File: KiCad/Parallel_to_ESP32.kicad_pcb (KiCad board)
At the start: 2 copper layers, 47 x 50 mm, 9 parts, among them J1 DB25_Male, J3 Micro_SD_Card_Socket, U1 ESP32-DEVKIT-V1

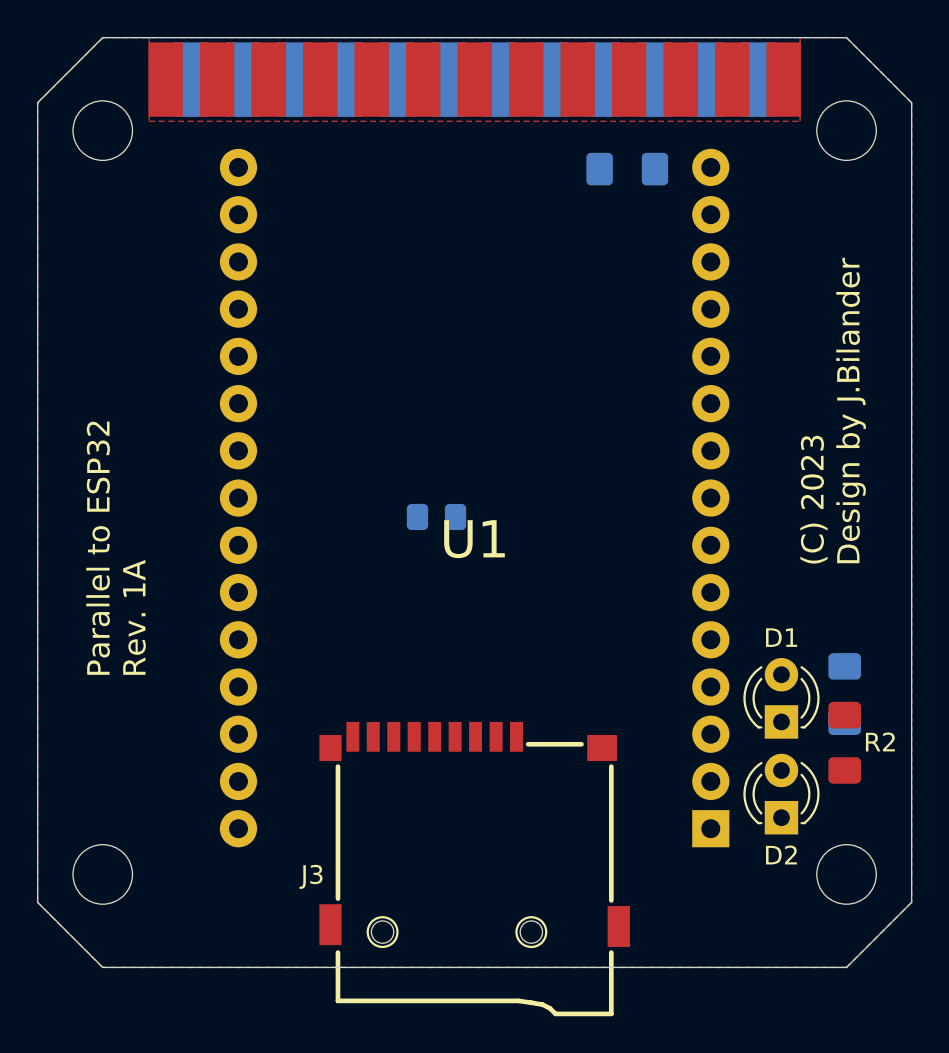
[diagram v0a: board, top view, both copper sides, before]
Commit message: placing of components and some routing done
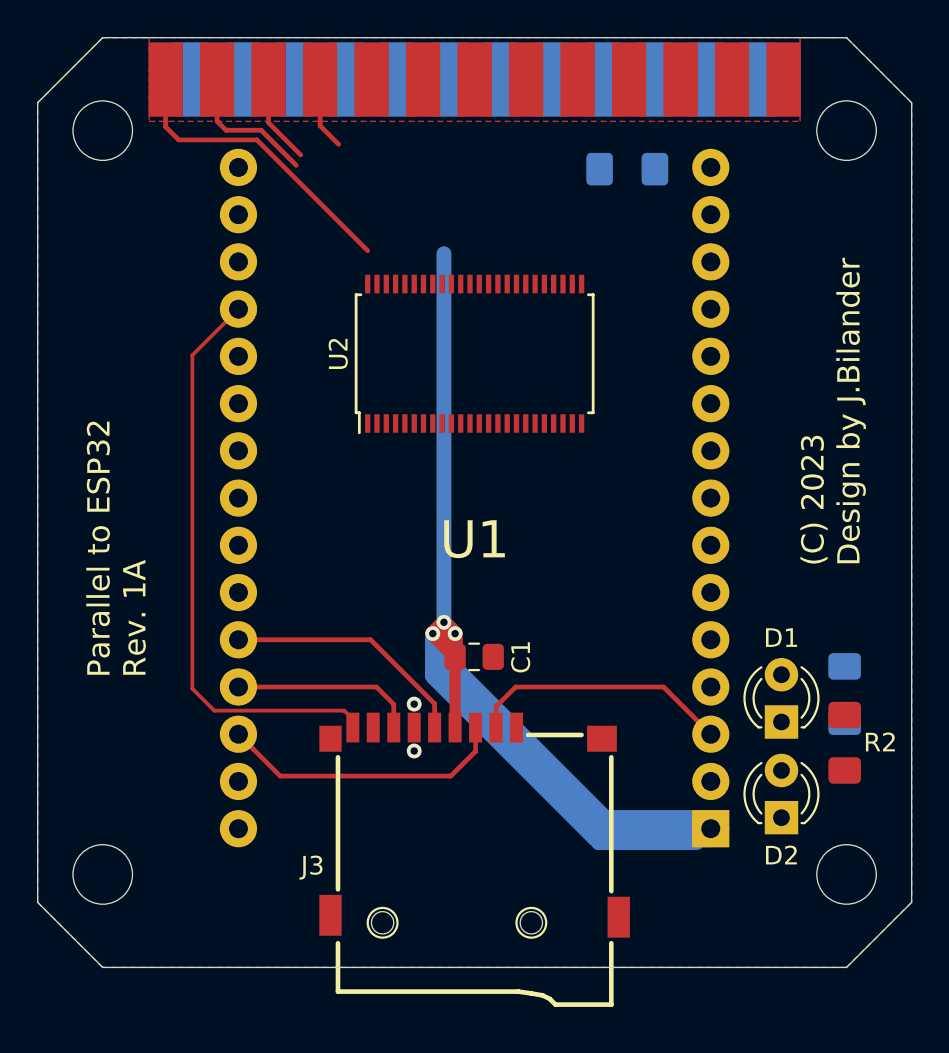
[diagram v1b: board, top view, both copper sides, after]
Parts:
- added U2: SN74CB3T16210, Package_SO:TSSOP-48_6.1x12.5mm_P0.5mm, F.Cu at (147.7, 102.0)
- C1: renamed from C4; moved to F.Cu
- moved C1 7.79 mm to (147.7, 118.3), turned to 0 degrees
- moved J3 0.50 mm to (147.7, 121.3)
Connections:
- D1 pad 2: VCC -> 3V3
- J3 pad 9: CP -> CD
- R2 pad 1: VCC -> 3V3
- U1 pad 1: Net-(U1-Pad1) -> 3V3
- U1 pad 19: Net-(U1-Pad19) -> CD
- U1 pad 2: Net-(U1-Pad2) -> GND
- U1 pad 26: Net-(U1-Pad26) -> SCK
- U1 pad 27: Net-(U1-Pad27) -> MISO
- U1 pad 28: Net-(U1-Pad28) -> MOSI
- U1 pad 29: Net-(U1-Pad2) -> GND
- U1 pad 3: Net-(U1-Pad3) -> CS
- U1 pad 30: Net-(U1-Pad30) -> VCC
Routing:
- net 3V3: track 0.00 -> 72.3 mm, vias 0 -> 3
- net CD: track 0.00 -> 31.2 mm
- net SELECT: track 0.00 -> 16.2 mm
- net MOSI: track 0.00 -> 15.5 mm
- net CS: track 0.00 -> 14.7 mm
- net SCK: track 0.00 -> 13.8 mm
- net MISO: track 0.00 -> 9.99 mm
- net POUT: track 0.00 -> 7.49 mm
- net BUSY: track 0.00 -> 4.77 mm
- net ACK: track 0.00 -> 3.90 mm
- net GND: vias 0 -> 2
- added copper zone on F.Cu, net GND
- removed copper zone on F.Cu, net VCC

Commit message: more routing done
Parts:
- moved JP1 12.1 mm to (167.5, 95.5)
- turned U2 to 270 degrees
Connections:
- net Net-(J1-Pad14) renamed Amiga_5V
- net Net-(U2-Pad25) renamed SELECT_3V3
- net Net-(U2-Pad26) renamed POUT_3V3
- net Net-(U2-Pad27) renamed BUSY_3V3
- net Net-(U2-Pad28) renamed ACK_3V3
- net Net-(U2-Pad36) renamed D7_3V3
- net Net-(U2-Pad37) renamed D6_3V3
- net Net-(U2-Pad38) renamed D5_3V3
- net Net-(U2-Pad39) renamed D4_3V3
- net Net-(U2-Pad40) renamed D3_3V3
- net Net-(U2-Pad42) renamed D2_3V3
- net Net-(U2-Pad43) renamed D1_3V3
- net Net-(U2-Pad44) renamed D0_3V3
- net Net-(U2-Pad45) renamed STROBE_3V3
- net Net-(U2-Pad46) renamed RESET_3V3
- net VCC renamed Net-(U1-Pad30)
- J1 pad 1: Net-(J1-Pad1) -> STROBE
- JP1 pad 2: RESET -> Net-(JP1-Pad2)
- U2 pad 10: Net-(U2-Pad10) -> D5
- U2 pad 11: Net-(U2-Pad11) -> D6
- U2 pad 12: Net-(U2-Pad12) -> D7
- U2 pad 13: Net-(U2-Pad13) -> GND
- U2 pad 14: Net-(U2-Pad14) -> GND
- U2 pad 16: Net-(U2-Pad16) -> GND
- U2 pad 18: Net-(U2-Pad18) -> GND
- U2 pad 19: Net-(U2-Pad19) -> GND
- U2 pad 2: Net-(U2-Pad2) -> RESET
- U2 pad 20: Net-(U2-Pad20) -> GND
- U2 pad 21: Net-(U2-Pad21) -> ACK
- U2 pad 22: Net-(U2-Pad22) -> BUSY
- U2 pad 23: Net-(U2-Pad23) -> POUT
- U2 pad 24: Net-(U2-Pad24) -> SELECT
- U2 pad 3: Net-(U2-Pad3) -> STROBE
- U2 pad 4: Net-(U2-Pad4) -> D0
- U2 pad 5: Net-(U2-Pad5) -> D1
- U2 pad 6: Net-(U2-Pad6) -> D2
- U2 pad 7: Net-(U2-Pad7) -> D3
- U2 pad 9: Net-(U2-Pad9) -> D4
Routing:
- net STROBE: track 0.00 -> 18.4 mm
- net D0: track 0.00 -> 16.3 mm
- net D1: track 0.00 -> 14.0 mm
- net D7: track 0.00 -> 13.4 mm
- net RESET: track 0.00 -> 13.2 mm, vias 0 -> 1
- net D2: track 0.00 -> 13.1 mm
- net D6: track 0.00 -> 12.5 mm
- net D3: track 0.00 -> 12.2 mm
- net D5: track 0.00 -> 11.5 mm
- net D4: track 0.00 -> 11.4 mm
- net BUSY: track 4.77 -> 13.6 mm
- net ACK: track 3.90 -> 12.7 mm
- net POUT: track 7.49 -> 15.7 mm
- net SELECT: track 16.2 -> 17.8 mm
- net GND: vias 2 -> 12
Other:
- net class Default: trace_width 0.25 -> 0.254

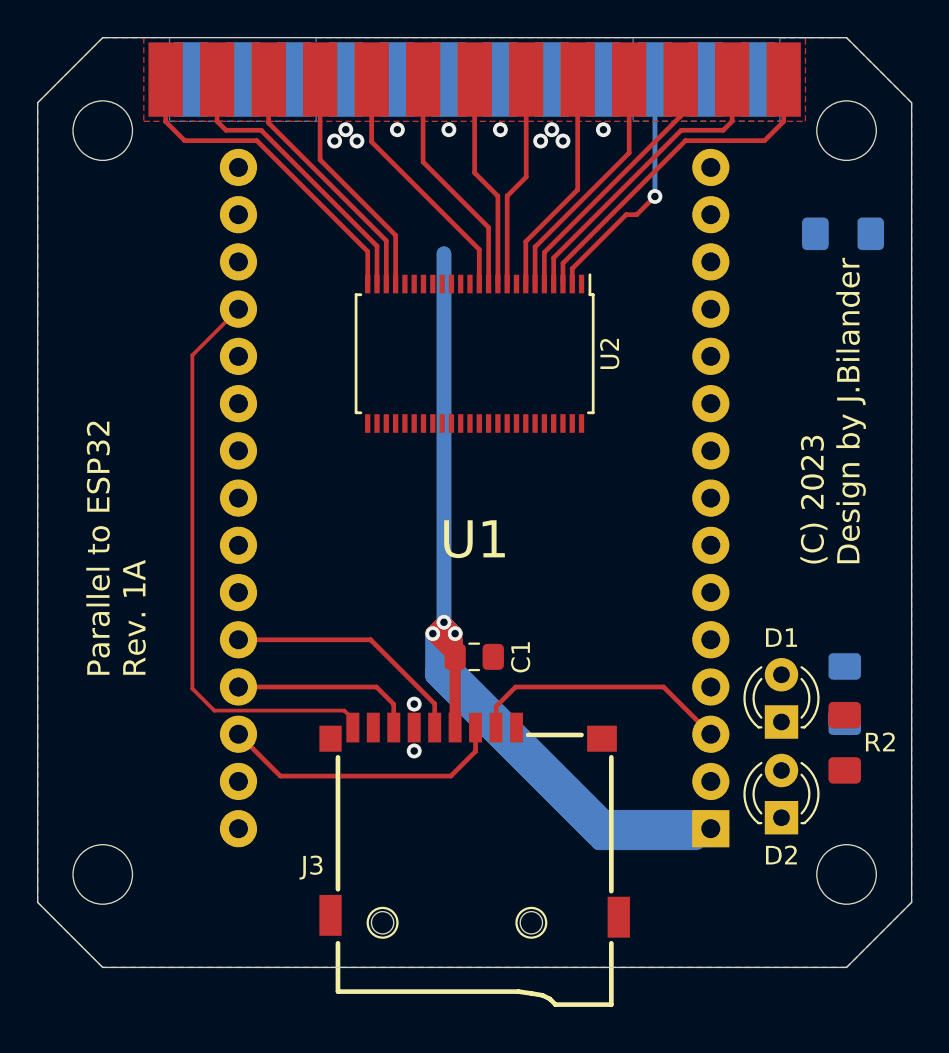
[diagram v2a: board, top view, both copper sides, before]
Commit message: more pin assignments and routing
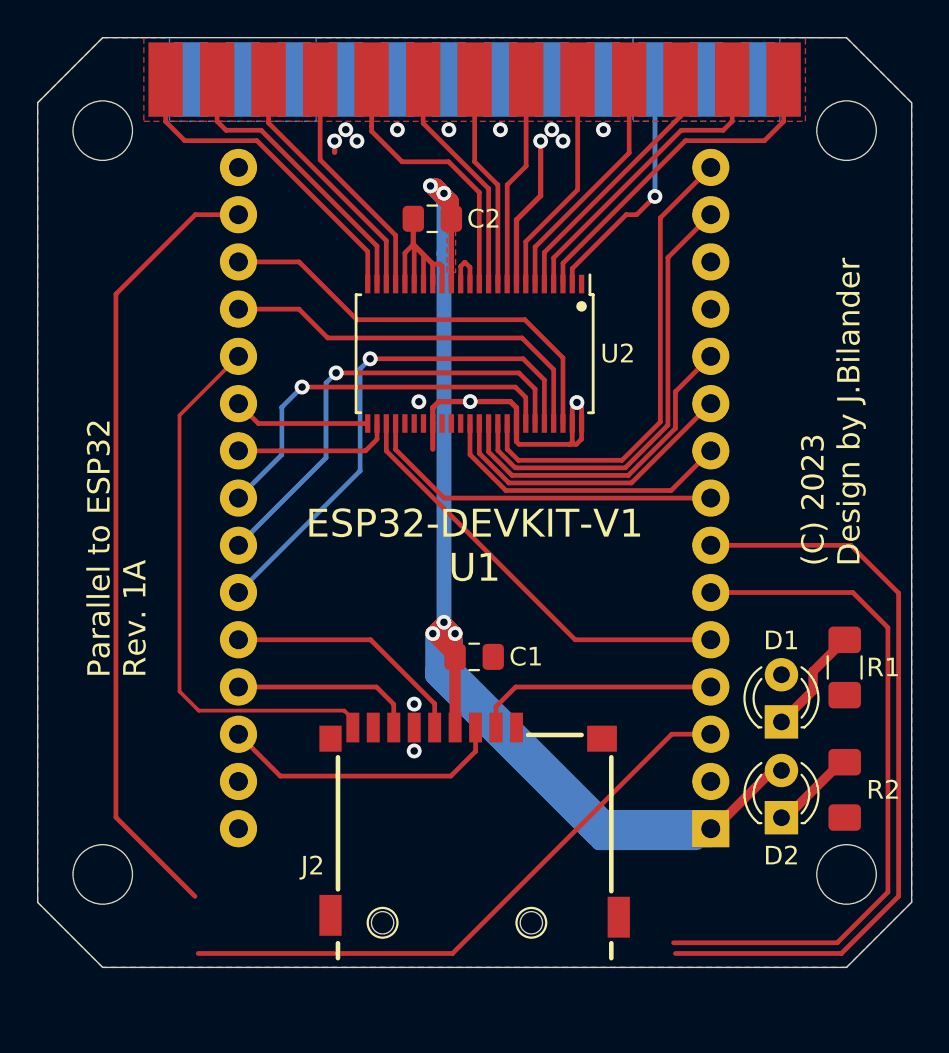
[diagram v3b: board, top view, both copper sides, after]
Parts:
- removed JP1: Jumper_2_Open, Resistor_SMD:R_1206_3216Metric_Pad1.42x1.75mm_HandSolder
- added C2: 0.1uF, Capacitor_SMD:C_0805_2012Metric_Pad1.15x1.40mm_HandSolder, F.Cu at (145.4, 94.7)
- R1: moved to F.Cu
- moved R2 2.53 mm to (167.6, 125.5)
- moved R1 1.43 mm to (167.6, 118.9), turned to 270 degrees
- renumbered J3 to J2
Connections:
- net Net-(U1-Pad12) renamed RX0
- net Net-(U1-Pad13) renamed TX0
- net Net-(U1-Pad17) renamed RX1
- net Net-(U1-Pad6) renamed RX2
- net Net-(U1-Pad7) renamed TX2
- D1 pad 2: 3V3 -> ACT_LED
- D2 pad 1: GND -> Net-(D2-Pad1)
- D2 pad 2: Net-(D2-Pad2) -> 3V3
- R1 pad 2: ACT_LED -> GND
- R2 pad 1: 3V3 -> Net-(D2-Pad1)
- R2 pad 2: Net-(D2-Pad2) -> GND
- U1 pad 10: Net-(U1-Pad10) -> D6_3V3
- U1 pad 11: Net-(U1-Pad11) -> D5_3V3
- U1 pad 14: Net-(U1-Pad14) -> D4_3V3
- U1 pad 15: Net-(U1-Pad15) -> D3_3V3
- U1 pad 18: Net-(U1-Pad18) -> RESET_3V3
- U1 pad 19: CD -> STROBE_3V3
- U1 pad 20: Net-(U1-Pad20) -> CD
- U1 pad 21: Net-(U1-Pad21) -> SELECT_3V3
- U1 pad 22: Net-(U1-Pad22) -> POUT_3V3
- U1 pad 23: Net-(U1-Pad23) -> D2_3V3
- U1 pad 24: Net-(U1-Pad24) -> D1_3V3
- U1 pad 25: Net-(U1-Pad25) -> D0_3V3
- U1 pad 3: CS -> TX1
- U1 pad 4: Net-(U1-Pad4) -> CS
- U1 pad 5: Net-(U1-Pad5) -> BUSY_3V3
- U1 pad 8: Net-(U1-Pad8) -> ACK_3V3
- U1 pad 9: Net-(U1-Pad9) -> D7_3V3
- U2 pad 47: Net-(U2-Pad47) -> GND
- U2 pad 48: Net-(U2-Pad48) -> GND
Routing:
- net RX1: track 0.00 -> 42.5 mm
- net TX2: track 0.00 -> 40.7 mm
- net GND: track 0.00 -> 40.6 mm, vias 12 -> 15
- net RX2: track 0.00 -> 37.2 mm
- net TX1: track 0.00 -> 32.5 mm
- net D0_3V3: track 0.00 -> 27.7 mm, vias 0 -> 1
- net D3_3V3: track 0.00 -> 25.5 mm
- net D1_3V3: track 0.00 -> 24.4 mm, vias 0 -> 1
- net D4_3V3: track 0.00 -> 24.2 mm
- net BUSY_3V3: track 0.00 -> 23.1 mm
- net RESET_3V3: track 0.00 -> 23.1 mm
- net STROBE_3V3: track 0.00 -> 21.2 mm
- net D2_3V3: track 0.00 -> 21.0 mm, vias 0 -> 1
- net ACK_3V3: track 0.00 -> 19.4 mm
- net 3V3: track 72.3 -> 91.1 mm, vias 3 -> 5
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- added copper zone on F.Cu, net 3V3
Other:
- board text added: "ESP32-DEVKIT-V1"

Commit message: Added pinheader for UART1
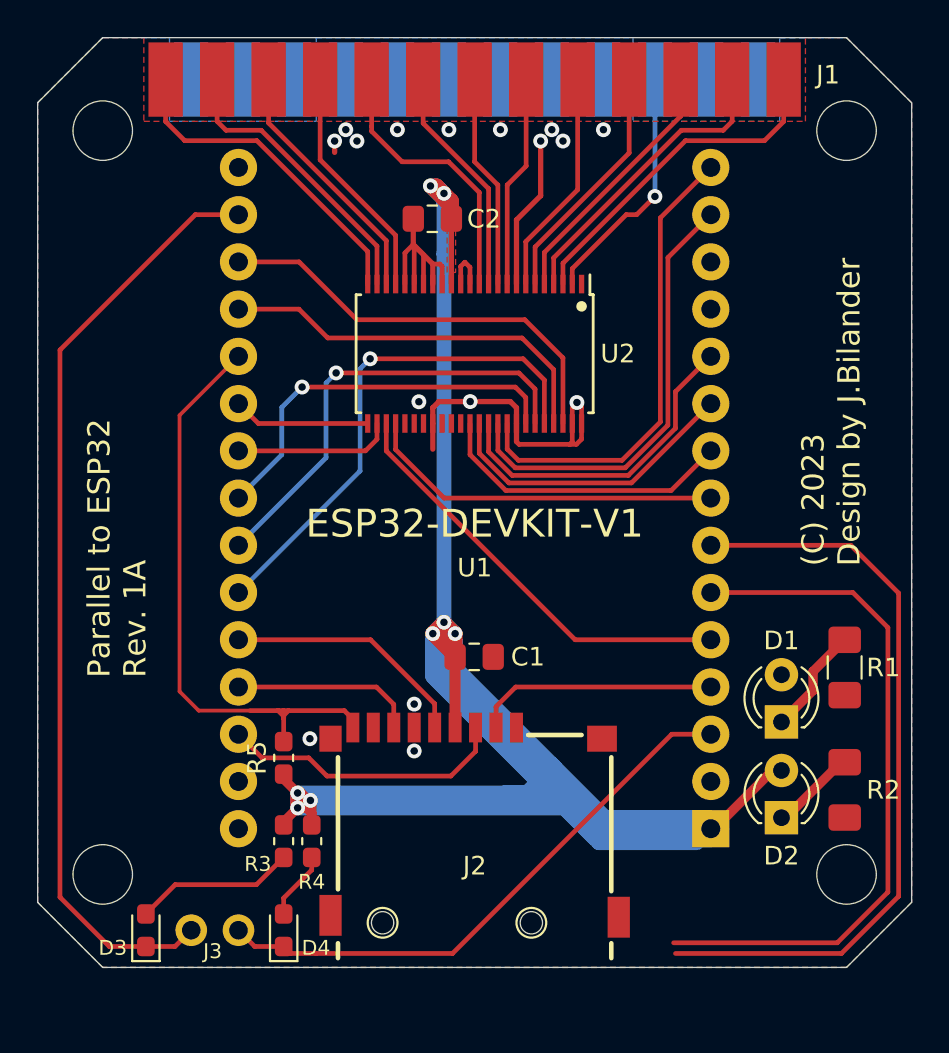
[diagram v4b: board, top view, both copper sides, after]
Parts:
- added D3: LED, Diode_SMD:D_0603_1608Metric_Pad1.05x0.95mm_HandSolder, F.Cu at (130.0, 133.0)
- added D4: LED, Diode_SMD:D_0603_1608Metric_Pad1.05x0.95mm_HandSolder, F.Cu at (137.4, 133.0)
- added J3: Conn_01x02, Connector_PinHeader_2.54mm:PinHeader_1x02_P2.54mm_Vertical, F.Cu at (135.0, 133.0)
- added R3: 1k, Resistor_SMD:R_0603_1608Metric_Pad1.05x0.95mm_HandSolder, F.Cu at (137.4, 128.2)
- added R4: 1k, Resistor_SMD:R_0603_1608Metric_Pad1.05x0.95mm_HandSolder, F.Cu at (138.9, 128.2)
- added R5: 1k, Resistor_SMD:R_0603_1608Metric_Pad1.05x0.95mm_HandSolder, F.Cu at (137.4, 123.7)
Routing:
- net 3V3: track 91.1 -> 148.8 mm, vias 5 -> 8
- net Net-(D3-Pad2): track 0.00 -> 8.67 mm
- net RX1: track 42.5 -> 50.6 mm
- net Net-(D4-Pad2): track 0.00 -> 3.67 mm
- net CD: track 29.7 -> 32.4 mm
- net TX1: track 32.5 -> 31.4 mm
- net GND: vias 15 -> 16

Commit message: Added pinheader for UART2
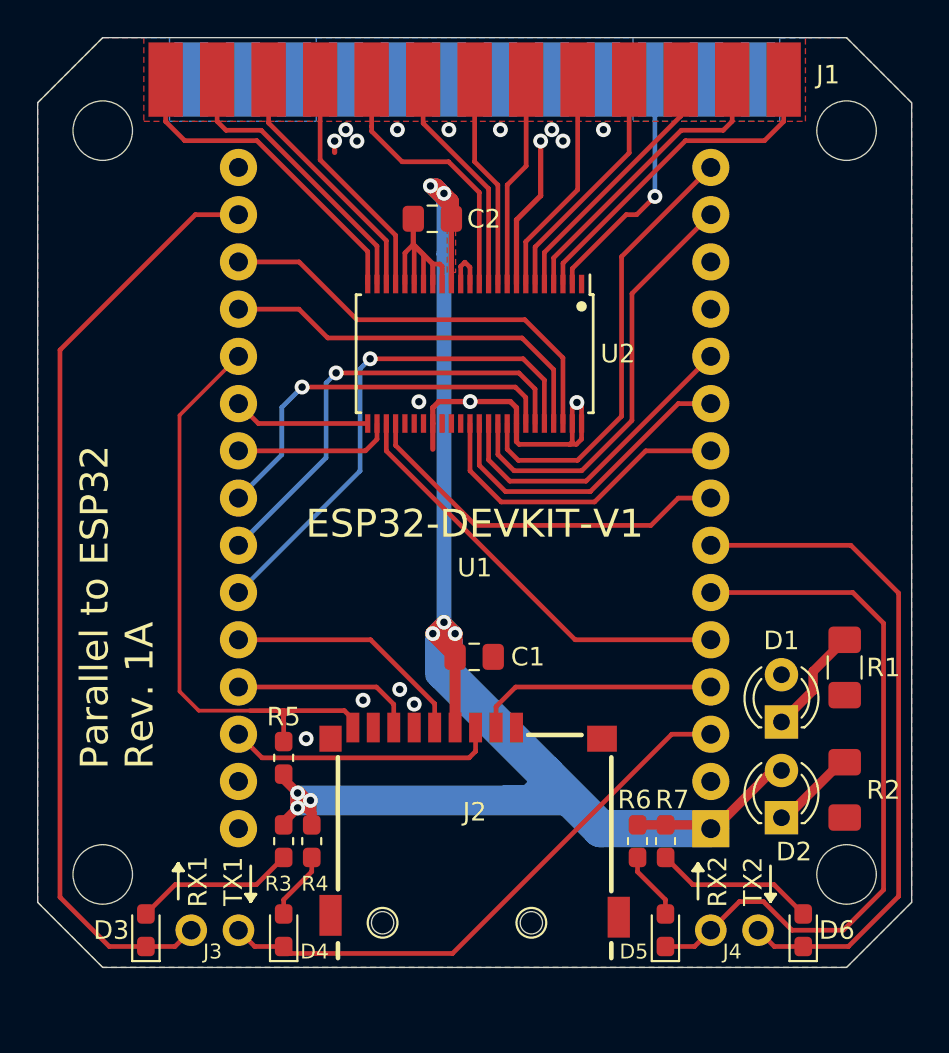
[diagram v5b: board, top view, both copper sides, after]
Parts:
- added D5: LED, Diode_SMD:D_0603_1608Metric_Pad1.05x0.95mm_HandSolder, F.Cu at (158.0, 133.0)
- added D6: LED, Diode_SMD:D_0603_1608Metric_Pad1.05x0.95mm_HandSolder, F.Cu at (165.4, 133.0)
- added J4: Conn_01x02, Connector_PinHeader_2.54mm:PinHeader_1x02_P2.54mm_Vertical, F.Cu at (162.9, 133.0)
- added R6: 1k, Resistor_SMD:R_0603_1608Metric_Pad1.05x0.95mm_HandSolder, F.Cu at (156.5, 128.2)
- added R7: 1k, Resistor_SMD:R_0603_1608Metric_Pad1.05x0.95mm_HandSolder, F.Cu at (158.0, 128.2)
- R5: value 1k -> 10k
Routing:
- net 3V3: track 148.8 -> 134.9 mm
- net Net-(D6-Pad2): track 0.00 -> 8.67 mm
- net TX2: track 40.7 -> 36.5 mm
- net Net-(D5-Pad2): track 0.00 -> 3.66 mm
- net D3_3V3: track 25.5 -> 24.1 mm
- net RX2: track 37.2 -> 38.6 mm
- net ACK_3V3: track 19.4 -> 20.5 mm
- net D4_3V3: track 24.2 -> 23.2 mm
- net D7_3V3: track 16.3 -> 17.3 mm
- net MOSI: track 15.5 -> 14.7 mm
- net D6_3V3: track 16.5 -> 17.2 mm
- net D5_3V3: track 17.8 -> 17.2 mm
- net GND: vias 16 -> 17
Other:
- board text added: "RX1"
- board text added: "RX2"
- board text added: "TX1"
- board text added: "TX2"

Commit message: Changed R2 resistor to 0805-footprint and did some routing fixes
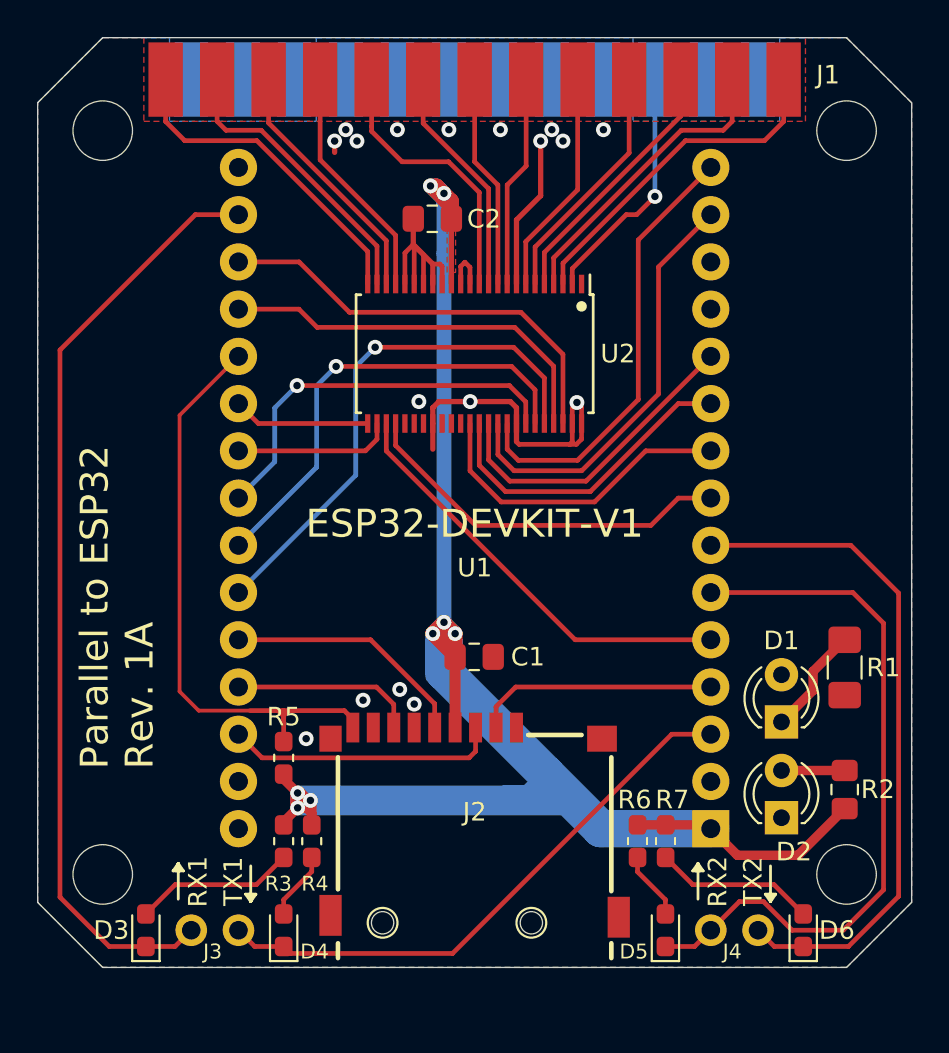
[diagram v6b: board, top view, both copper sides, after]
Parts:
- R2: footprint Resistor_SMD:R_1206_3216Metric_Pad1.42x1.75mm_HandSolder -> Resistor_SMD:R_0805_2012Metric_Pad1.15x1.40mm_HandSolder
- turned R2 to 90 degrees
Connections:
- D2 pad 1: Net-(D2-Pad1) -> GND
- D2 pad 2: 3V3 -> Net-(D2-Pad2)
- R2 pad 1: Net-(D2-Pad1) -> 3V3
- R2 pad 2: GND -> Net-(D2-Pad2)
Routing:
- net 3V3: track 134.9 -> 140.2 mm
- net Net-(D2-Pad1): track 4.64 -> 0.00 mm
- net Net-(D2-Pad2): track 0.00 -> 3.40 mm
- net D0_3V3: track 27.7 -> 28.5 mm
